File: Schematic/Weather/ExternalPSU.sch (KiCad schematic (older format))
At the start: 2 parts

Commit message: schematic changes
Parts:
- gave numbers to parts that had none: 2
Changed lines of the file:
@@
 J5_P3
 $Comp
-L MyComponents:PowerBrick PSU?
+L MyComponents:PowerBrick PSU2
 U 1 1 5C96411B
 P 4050 2100
-F 0 "PSU?" H 4678 2121 50  0000 L CNN
+F 0 "PSU2" H 4678 2121 50  0000 L CNN
 F 1 "PowerBrick" H 4678 2030 50  0000 L CNN
 F 2 "" H 4250 1800 50  0001 C CNN
@@
 $EndComp
 $Comp
-L MyComponents:PowerBrick PSU?
+L MyComponents:PowerBrick PSU3
 U 1 1 5C9656A9
 P 4050 2600
-F 0 "PSU?" H 4678 2621 50  0000 L CNN
+F 0 "PSU3" H 4678 2621 50  0000 L CNN
 F 1 "PowerBrick" H 4678 2530 50  0000 L CNN
 F 2 "" H 4250 2300 50  0001 C CNN

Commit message: Start PCB
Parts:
- PSU2, PSU3: footprint (none) -> footprint:PowerBrick
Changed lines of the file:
@@
 F 0 "PSU2" H 4678 2121 50  0000 L CNN
 F 1 "PowerBrick" H 4678 2030 50  0000 L CNN
-F 2 "" H 4250 1800 50  0001 C CNN
+F 2 "footprint:PowerBrick" H 4250 1800 50  0001 C CNN
 F 3 "" H 4250 1800 50  0001 C CNN
 	1    4050 2100
@@
 F 0 "PSU3" H 4678 2621 50  0000 L CNN
 F 1 "PowerBrick" H 4678 2530 50  0000 L CNN
-F 2 "" H 4250 2300 50  0001 C CNN
+F 2 "footprint:PowerBrick" H 4250 2300 50  0001 C CNN
 F 3 "" H 4250 2300 50  0001 C CNN
 	1    4050 2600

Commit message: more changes
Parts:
- added J3: 3_Way_Wire, Connector_PinHeader_2.54mm:PinHeader_1x03_P2.54mm_Vertical, symbol MyComponents:3_Way_Wire
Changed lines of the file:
@@
 $Descr A4 11693 8268
 encoding utf-8
-Sheet 5 14
+Sheet 5 15
 Title ""
 Date ""
@@
 $EndComp
 Wire Wire Line
-	2500 2500 3950 2500
-Wire Wire Line
 	2500 2250 3500 2250
 Wire Wire Line
@@
 Wire Wire Line
 	3750 2750 3950 2750
+Wire Wire Line
+	3950 2500 2500 2500
+$Comp
+L MyComponents:3_Way_Wire J3
+U 1 1 5CB57954
+P 3300 1350
+F 0 "J3" H 3469 1311 50  0000 L CNN
+F 1 "3_Way_Wire" H 3469 1220 50  0000 L CNN
+F 2 "Connector_PinHeader_2.54mm:PinHeader_1x03_P2.54mm_Vertical" H 3300 1350 50  0001 C CNN
+F 3 "" H 3300 1350 50  0001 C CNN
+	1    3300 1350
+	1    0    0    -1
+$EndComp
 $EndSCHEMATC

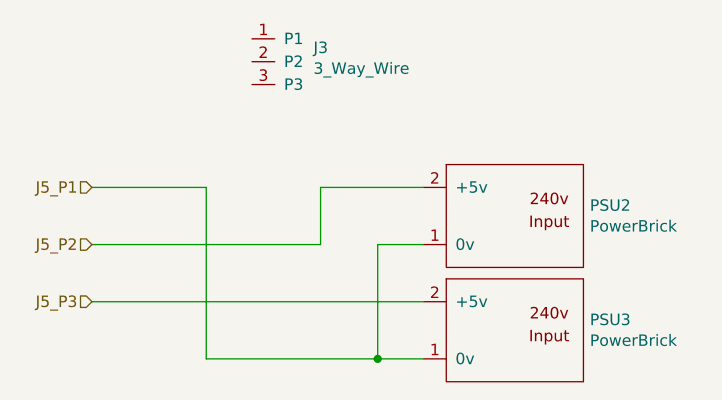
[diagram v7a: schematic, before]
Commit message: Connector relable start
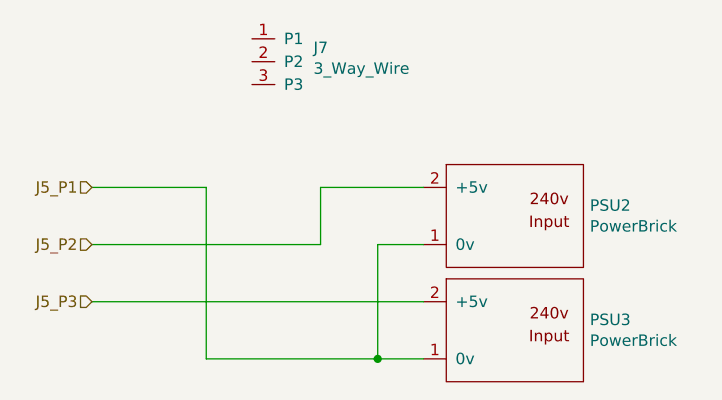
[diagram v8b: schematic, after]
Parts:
- renumbered J3 to J7
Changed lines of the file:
@@
 	3950 2500 2500 2500
 $Comp
-L MyComponents:3_Way_Wire J3
+L MyComponents:3_Way_Wire J7
 U 1 1 5CB57954
 P 3300 1350
-F 0 "J3" H 3469 1311 50  0000 L CNN
+F 0 "J7" H 3469 1311 50  0000 L CNN
 F 1 "3_Way_Wire" H 3469 1220 50  0000 L CNN
 F 2 "Connector_PinHeader_2.54mm:PinHeader_1x03_P2.54mm_Vertical" H 3300 1350 50  0001 C CNN
